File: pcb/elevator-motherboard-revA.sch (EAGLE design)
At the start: 55 parts, among them J3 MAGJACK, J4 MAGJACK, J5 MAGJACK, J6 POWER_JACK, J8 MAGJACK, Q1 NCV8403BDTRKG, Q2 MOSFET_NCH_DUAL-SO08, Q3 MOSFET_NCH_DUAL-SO08, Q4 MOSFET_NCH_DUAL-SO08, Q5 NCV8403BDTRKG, Q6 MOSFET_NCH_DUAL-SO08, Q7 NCV8403BDTRKG, Q8 NCV8403BDTRKG, Q9 NCV8403BDTRKG, U2 TPD2E001, U3 TPD2E001, U4 74HC2G125, U5 TPD2E001, U7 TPD2E001

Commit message: motherboard schematic is done
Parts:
- removed C19: 0.1uF, microbuilder:CAP_CERAMIC0603
- removed OUT4: MC4, con-phoenix-381_l:MC4
- removed PP3, PP4: MC2, con-phoenix-381_l:MC2
- added J1, J10, J7: (no value), SparkFun-Connectors:CONN_03
- added J9: (no value), SparkFun-Connectors:CONN_06NO_SILK_FEMALE_PTH
- added LED1, LED2, LED3, LED4: LED-GREEN0603, BeagleBone_Blue_R3:LED-GREEN0603
- added OUT1, OUT2: MC4, con-phoenix-381_l:MC4
- added R10, R13, R14, R7, R8, R9: (no value), adafruit:R-US_R0603
- added X1, X2, X3, X4: MSTBA2, con-phoenix-508:MSTBA2
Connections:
- new net B2B_RX1: J9.5, U$1.0/RX
- new net B2B_RX2: J9.6, U$1.2
- new net B2B_TX1: J9.3, U$1.1/TX
- new net B2B_TX2: J9.4, U$1.3/CANTX
- new net BOARD_ID: J10.2, U$1.15/A1
- new net IO1: J2.1, U$1.4/CANRX
- new net IO2: J2.2, U$1.5
- new net IO3: J2.3, U$1.6
- new net IO4: J2.4, U$1.7
- new net IO5: J2.5, U$1.12/MISO
- new net IO6: J2.6, U$1.24
- new net IO7: J2.7, U$1.25
- new net IO8: J2.8, U$1.26
- new net IO9: J2.9, U$1.27
- new net N$23: LED1.A, R9.1
- new net N$24: LED2.A, R10.1
- new net N$25: LED3.A, R7.1
- new net N$26: LED4.A, R8.1
- new net N$27: J10.3, R13.1
- new net N$33: J10.1, R14.2
- new net N$50: U$1.23/A9
- new net N$51: U$1.22/A8
- new net N$60: U$1.13/SCK
- new net N$61: U$1.GND2
- net 12V: now also J1.1, J2.10, J7.1, J7.2, OUT1.1.SK, R8.2, X3-1.1; no longer OUT4.4.SK
- net 24V: now also J1.2, J1.3, J7.3, OUT1.4.SK, OUT2.4.SK, R10.2, X1-1.1, X2-1.1; no longer PP3.1.SK, PP4.1.SK
- net 5V: now also OUT2.1.SK, R7.2, U$1.VIN, X4-1.1; no longer OUT4.1.SK
- net A.M1: now also U$1.30
- net A.M2: now also U$1.31/A12
- net A.SW1: now also U$1.28
- net A.SW2: now also U$1.29
- net B.M1: now also U$1.34/A15
- net B.M2: now also U$1.33/A14
- net B.SW1: now also U$1.32/A13
- net B.SW2: now also U$1.35/A16
- net C.M1: now also U$1.37/A18
- net C.M2: now also U$1.36/A17
- net C.SW1: now also U$1.39/A20
- net C.SW2: now also U$1.38/A19
- net D.M1: now also U$1.19/A5/SCL
- net D.M2: now also U$1.18/A4/SDA
- net D.SW1: now also U$1.9/CS
- net D.SW2: now also U$1.11/MOSI
- net GND: now also J2.12, J9.2, LED1.C, LED2.C, LED3.C, LED4.C, OUT1.2.SK, OUT1.3.SK, OUT2.2.SK, OUT2.3.SK, R14.1, X1-2.1, X2-2.1, X3-2.1, X4-2.1; no longer OUT4.2.SK, OUT4.3.SK, PP3.2.SK, PP4.2.SK
- net LEDS1: now also U$1.8
- net LEDS2: now also U$1.10/CS
- net PWM1: now also U$1.14/A0
- net PWM2: now also U$1.16/A2
- net PWM3: now also U$1.17/A3
- net PWM4: now also U$1.20/A6
- net PWM5: now also U$1.21/A7
- net VCC: now also J2.11, J9.1, R13.2, R9.2
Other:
- note added: "B2B"
- note added: "Door controller D conflicts with audio shield pins. Use one or the other!"
- note added: "Door controllers + limit switches"
- note added: "IO Panel"
- note added: "Individually addressable LEDs"
- note added: "MCU"
- note added: "PWM LEDs"
- note added: "Power rails"
- moved on the sheet: C1, C10, C11, C12, C13, C17, C18, C20, C4, C5, C6, C7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

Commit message: backup
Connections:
- new net N$34: J7.2, PP1.1.SK
- net 12V: no longer J7.2, PP1.1.SK
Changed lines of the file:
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@@
 <net name="12V" class="0">
-<segment>
-<pinref part="PP1" gate=".1" pin="SK"/>
-<wire x1="256.54" y1="320.04" x2="259.08" y2="320.04" width="0.1524" layer="91"/>
-<pinref part="J7" gate="J$1" pin="2"/>
-<wire x1="256.54" y1="320.04" x2="256.54" y2="337.82" width="0.1524" layer="91"/>
-<wire x1="256.54" y1="337.82" x2="248.92" y2="337.82" width="0.1524" layer="91"/>
-</segment>
 <segment>
 <pinref part="OUT1" gate=".1" pin="SK"/>
@@
 </segment>
 </net>
+<net name="N$34" class="0">
+<segment>
+<pinref part="J7" gate="J$1" pin="2"/>
+<pinref part="PP1" gate=".1" pin="SK"/>
+<wire x1="248.92" y1="337.82" x2="248.92" y2="320.04" width="0.1524" layer="91"/>
+<wire x1="248.92" y1="320.04" x2="259.08" y2="320.04" width="0.1524" layer="91"/>
+</segment>
+</net>

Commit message: wip
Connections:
- new net N$35: J1.2, PP2.1.SK
- net 24V: no longer J1.2, PP2.1.SK
- net GND: now also Q5.S, Q7.S, Q8.S, Q9.S
- net N$5: now also PL2.2.SK; no longer PL1.2.SK
- net N$6: now also PL1.2.SK; no longer PL2.2.SK
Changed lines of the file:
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@@
 <part name="R14" library="adafruit" library_urn="urn:adsk.eagle:library:420" deviceset="R-US_" device="R0603" package3d_urn="urn:adsk.eagle:package:6240565/1"/>
 <part name="GND12" library="SparkFun-Aesthetics" deviceset="GND" device=""/>
+<part name="U$2" library="SparkFun-PowerSymbols" library_urn="urn:adsk.eagle:library:530" deviceset="AGND" device="" value="GND"/>
 </parts>
 <sheets>
@@
 <attribute name="VALUE" x="157.48" y="15.24" size="1.778" layer="96"/>
 </instance>
+<instance part="U$2" gate="G$1" x="223.52" y="220.98" smashed="yes">
+<attribute name="VALUE" x="223.52" y="220.726" size="1.778" layer="96" align="top-center"/>
+</instance>
 </instances>
 <busses>
@@
 <wire x1="160.02" y1="20.32" x2="160.02" y2="25.4" width="0.1524" layer="91"/>
 </segment>
+<segment>
+<pinref part="U$2" gate="G$1" pin="AGND"/>
+<pinref part="Q5" gate="G$1" pin="S"/>
+<wire x1="213.36" y1="269.24" x2="223.52" y2="269.24" width="0.1524" layer="91"/>
+<wire x1="223.52" y1="269.24" x2="223.52" y2="254" width="0.1524" layer="91"/>
+<pinref part="Q7" gate="G$1" pin="S"/>
+<wire x1="223.52" y1="254" x2="223.52" y2="238.76" width="0.1524" layer="91"/>
+<wire x1="223.52" y1="238.76" x2="223.52" y2="223.52" width="0.1524" layer="91"/>
+<wire x1="213.36" y1="254" x2="223.52" y2="254" width="0.1524" layer="91"/>
+<junction x="223.52" y="254"/>
+<pinref part="Q8" gate="G$1" pin="S"/>
+<wire x1="213.36" y1="238.76" x2="223.52" y2="238.76" width="0.1524" layer="91"/>
+<junction x="223.52" y="238.76"/>
+<pinref part="Q9" gate="G$1" pin="S"/>
+<wire x1="213.36" y1="223.52" x2="223.52" y2="223.52" width="0.1524" layer="91"/>
+<junction x="223.52" y="223.52"/>
+</segment>
 </net>
 <net name="12V" class="0">
@@
 </segment>
 </net>
-<net name="N$5" class="0">
-<segment>
-<pinref part="U4" gate="G$1" pin="1Y"/>
-<wire x1="220.98" y1="137.16" x2="238.76" y2="137.16" width="0.1524" layer="91"/>
-<wire x1="238.76" y1="149.86" x2="238.76" y2="137.16" width="0.1524" layer="91"/>
-<pinref part="PL1" gate=".2" pin="SK"/>
-<wire x1="238.76" y1="149.86" x2="271.78" y2="149.86" width="0.1524" layer="91"/>
-</segment>
-</net>
-<net name="N$6" class="0">
-<segment>
-<pinref part="U4" gate="G$1" pin="2Y"/>
-<pinref part="PL2" gate=".2" pin="SK"/>
-<wire x1="271.78" y1="121.92" x2="259.08" y2="121.92" width="0.1524" layer="91"/>
-<wire x1="259.08" y1="121.92" x2="259.08" y2="129.54" width="0.1524" layer="91"/>
-<wire x1="259.08" y1="129.54" x2="220.98" y2="129.54" width="0.1524" layer="91"/>
-</segment>
-</net>
 <net name="LEDS1" class="0">
 <segment>
@@
 <net name="24V" class="0">
 <segment>
-<pinref part="PP2" gate=".1" pin="SK"/>
-<wire x1="256.54" y1="266.7" x2="261.62" y2="266.7" width="0.1524" layer="91"/>
-<pinref part="J1" gate="J$1" pin="2"/>
-<wire x1="251.46" y1="292.1" x2="256.54" y2="292.1" width="0.1524" layer="91"/>
-<wire x1="256.54" y1="292.1" x2="256.54" y2="266.7" width="0.1524" layer="91"/>
-</segment>
-<segment>
 <pinref part="J6" gate="G$1" pin="PWR"/>
 <wire x1="111.76" y1="320.04" x2="119.38" y2="320.04" width="0.1524" layer="91"/>
@@
 </segment>
 </net>
+<net name="N$35" class="0">
+<segment>
+<pinref part="J1" gate="J$1" pin="2"/>
+<wire x1="251.46" y1="292.1" x2="259.08" y2="292.1" width="0.1524" layer="91"/>
+<wire x1="259.08" y1="292.1" x2="259.08" y2="266.7" width="0.1524" layer="91"/>
+<pinref part="PP2" gate=".1" pin="SK"/>
+<wire x1="259.08" y1="266.7" x2="261.62" y2="266.7" width="0.1524" layer="91"/>
+</segment>
+</net>
+<net name="N$5" class="0">
+<segment>
+<pinref part="U4" gate="G$1" pin="1Y"/>
+<wire x1="220.98" y1="137.16" x2="256.54" y2="137.16" width="0.1524" layer="91"/>
+<wire x1="256.54" y1="137.16" x2="256.54" y2="121.92" width="0.1524" layer="91"/>
+<pinref part="PL2" gate=".2" pin="SK"/>
+<wire x1="256.54" y1="121.92" x2="271.78" y2="121.92" width="0.1524" layer="91"/>
+</segment>
+</net>
+<net name="N$6" class="0">
+<segment>
+<pinref part="U4" gate="G$1" pin="2Y"/>
+<wire x1="220.98" y1="129.54" x2="241.3" y2="129.54" width="0.1524" layer="91"/>
+<wire x1="241.3" y1="129.54" x2="241.3" y2="149.86" width="0.1524" layer="91"/>
+<pinref part="PL1" gate=".2" pin="SK"/>
+<wire x1="241.3" y1="149.86" x2="271.78" y2="149.86" width="0.1524" layer="91"/>
+</segment>
+</net>

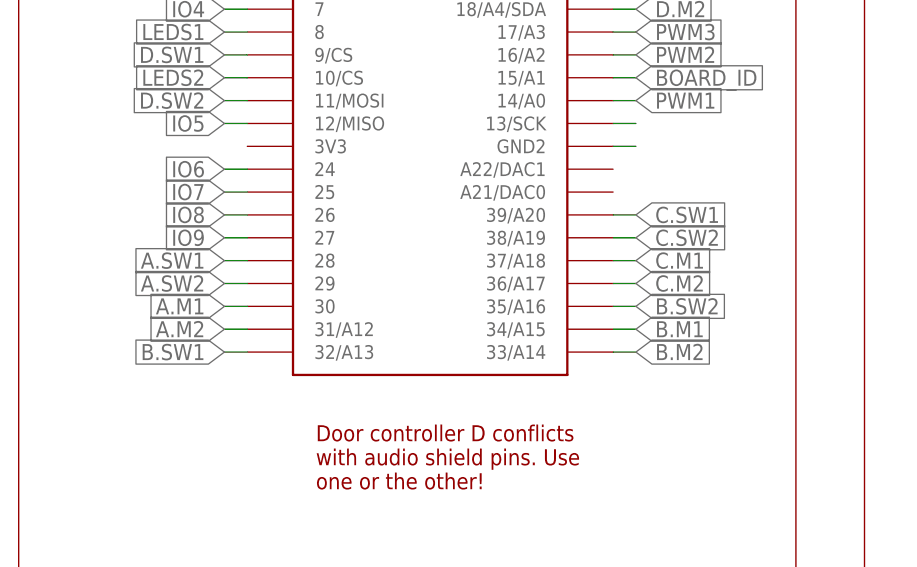
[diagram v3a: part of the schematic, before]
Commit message: better placement
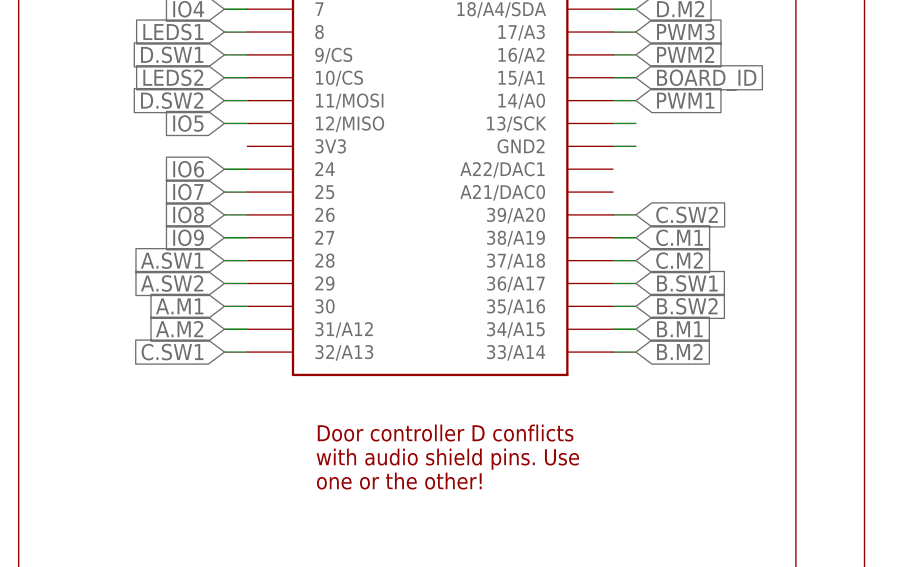
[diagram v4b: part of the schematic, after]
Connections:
- net B.SW1: now also U$1.36/A17; no longer U$1.32/A13
- net C.M1: now also U$1.38/A19; no longer U$1.37/A18
- net C.M2: now also U$1.37/A18; no longer U$1.36/A17
- net C.SW1: now also U$1.32/A13; no longer U$1.39/A20
- net C.SW2: now also U$1.39/A20; no longer U$1.38/A19
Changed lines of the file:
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@@
 </segment>
 <segment>
-<pinref part="U$1" gate="G$1" pin="32/A13"/>
-<wire x1="63.5" y1="30.48" x2="60.96" y2="30.48" width="0.1524" layer="91"/>
-<label x="60.96" y="30.48" size="1.778" layer="95" rot="R180" xref="yes"/>
+<pinref part="U$1" gate="G$1" pin="36/A17"/>
+<wire x1="104.14" y1="38.1" x2="106.68" y2="38.1" width="0.1524" layer="91"/>
+<label x="106.68" y="38.1" size="1.778" layer="95" xref="yes"/>
 </segment>
 </net>
@@
 </segment>
 <segment>
-<pinref part="U$1" gate="G$1" pin="39/A20"/>
-<wire x1="104.14" y1="45.72" x2="106.68" y2="45.72" width="0.1524" layer="91"/>
-<label x="106.68" y="45.72" size="1.778" layer="95" xref="yes"/>
+<pinref part="U$1" gate="G$1" pin="32/A13"/>
+<wire x1="63.5" y1="30.48" x2="60.96" y2="30.48" width="0.1524" layer="91"/>
+<label x="60.96" y="30.48" size="1.778" layer="95" rot="R180" xref="yes"/>
 </segment>
 </net>
@@
 </segment>
 <segment>
-<pinref part="U$1" gate="G$1" pin="38/A19"/>
-<wire x1="104.14" y1="43.18" x2="106.68" y2="43.18" width="0.1524" layer="91"/>
-<label x="106.68" y="43.18" size="1.778" layer="95" xref="yes"/>
+<pinref part="U$1" gate="G$1" pin="39/A20"/>
+<wire x1="104.14" y1="45.72" x2="106.68" y2="45.72" width="0.1524" layer="91"/>
+<label x="106.68" y="45.72" size="1.778" layer="95" xref="yes"/>
 </segment>
 </net>
@@
 </segment>
 <segment>
-<pinref part="U$1" gate="G$1" pin="37/A18"/>
-<wire x1="104.14" y1="40.64" x2="106.68" y2="40.64" width="0.1524" layer="91"/>
-<label x="106.68" y="40.64" size="1.778" layer="95" xref="yes"/>
+<pinref part="U$1" gate="G$1" pin="38/A19"/>
+<wire x1="104.14" y1="43.18" x2="106.68" y2="43.18" width="0.1524" layer="91"/>
+<label x="106.68" y="43.18" size="1.778" layer="95" xref="yes"/>
 </segment>
 </net>
@@
 </segment>
 <segment>
-<pinref part="U$1" gate="G$1" pin="36/A17"/>
-<wire x1="104.14" y1="38.1" x2="106.68" y2="38.1" width="0.1524" layer="91"/>
-<label x="106.68" y="38.1" size="1.778" layer="95" xref="yes"/>
+<pinref part="U$1" gate="G$1" pin="37/A18"/>
+<wire x1="104.14" y1="40.64" x2="106.68" y2="40.64" width="0.1524" layer="91"/>
+<label x="106.68" y="40.64" size="1.778" layer="95" xref="yes"/>
 </segment>
 </net>

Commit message: wip
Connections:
- removed net N$61: U$1.GND2
- net GND: now also U$1.GND, U$1.GND2
- net IO1: now also U$1.6; no longer U$1.4/CANRX
- net IO2: now also U$1.7; no longer U$1.5
- net IO3: now also U$1.5; no longer U$1.6
- net IO4: now also U$1.12/MISO; no longer U$1.7
- net IO5: now also U$1.4/CANRX; no longer U$1.12/MISO
- net IO7: now also U$1.27; no longer U$1.25
- net IO8: now also U$1.25; no longer U$1.26
- net IO9: now also U$1.26; no longer U$1.27
- net VCC: now also U$1.3V3
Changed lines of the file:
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@@
 <junction x="223.52" y="223.52"/>
+</segment>
+<segment>
+<pinref part="U$1" gate="G$1" pin="GND2"/>
+<wire x1="104.14" y1="53.34" x2="106.68" y2="53.34" width="0.1524" layer="91"/>
+<label x="106.68" y="53.34" size="1.778" layer="95" xref="yes"/>
+</segment>
+<segment>
+<pinref part="U$1" gate="G$1" pin="GND"/>
+<wire x1="63.5" y1="88.9" x2="60.96" y2="88.9" width="0.1524" layer="91"/>
+<label x="60.96" y="88.9" size="1.778" layer="95" rot="R180" xref="yes"/>
 </segment>
 </net>
@@
 <label x="160.02" y="60.96" size="2.54" layer="95" rot="R90" xref="yes"/>
 </segment>
+<segment>
+<pinref part="U$1" gate="G$1" pin="3V3"/>
+<wire x1="63.5" y1="53.34" x2="48.26" y2="53.34" width="0.1524" layer="91"/>
+<label x="48.26" y="53.34" size="1.778" layer="95" rot="R180" xref="yes"/>
+</segment>
 </net>
 <net name="N$1" class="0">
@@
 <net name="IO1" class="0">
 <segment>
+<pinref part="J2" gate="G$1" pin="1"/>
+<wire x1="203.2" y1="38.1" x2="198.12" y2="38.1" width="0.1524" layer="91"/>
+<label x="198.12" y="38.1" size="1.778" layer="95" rot="R180" xref="yes"/>
+</segment>
+<segment>
+<pinref part="U$1" gate="G$1" pin="6"/>
+<wire x1="63.5" y1="71.12" x2="60.96" y2="71.12" width="0.1524" layer="91"/>
+<label x="60.96" y="71.12" size="1.778" layer="95" rot="R180" xref="yes"/>
+</segment>
+</net>
+<net name="IO2" class="0">
+<segment>
+<pinref part="J2" gate="G$1" pin="2"/>
+<wire x1="218.44" y1="38.1" x2="223.52" y2="38.1" width="0.1524" layer="91"/>
+<label x="223.52" y="38.1" size="1.778" layer="95" xref="yes"/>
+</segment>
+<segment>
+<pinref part="U$1" gate="G$1" pin="7"/>
+<wire x1="63.5" y1="68.58" x2="60.96" y2="68.58" width="0.1524" layer="91"/>
+<label x="60.96" y="68.58" size="1.778" layer="95" rot="R180" xref="yes"/>
+</segment>
+</net>
+<net name="IO3" class="0">
+<segment>
+<pinref part="J2" gate="G$1" pin="3"/>
+<wire x1="203.2" y1="35.56" x2="198.12" y2="35.56" width="0.1524" layer="91"/>
+<label x="198.12" y="35.56" size="1.778" layer="95" rot="R180" xref="yes"/>
+</segment>
+<segment>
+<pinref part="U$1" gate="G$1" pin="5"/>
+<wire x1="63.5" y1="73.66" x2="60.96" y2="73.66" width="0.1524" layer="91"/>
+<label x="60.96" y="73.66" size="1.778" layer="95" rot="R180" xref="yes"/>
+</segment>
+</net>
+<net name="IO4" class="0">
+<segment>
+<pinref part="J2" gate="G$1" pin="4"/>
+<wire x1="218.44" y1="35.56" x2="223.52" y2="35.56" width="0.1524" layer="91"/>
+<label x="223.52" y="35.56" size="1.778" layer="95" xref="yes"/>
+</segment>
+<segment>
+<pinref part="U$1" gate="G$1" pin="12/MISO"/>
+<wire x1="63.5" y1="55.88" x2="60.96" y2="55.88" width="0.1524" layer="91"/>
+<label x="60.96" y="55.88" size="1.778" layer="95" rot="R180" xref="yes"/>
+</segment>
+</net>
+<net name="IO5" class="0">
+<segment>
+<pinref part="J2" gate="G$1" pin="5"/>
+<wire x1="203.2" y1="33.02" x2="198.12" y2="33.02" width="0.1524" layer="91"/>
+<label x="198.12" y="33.02" size="1.778" layer="95" rot="R180" xref="yes"/>
+</segment>
+<segment>
 <pinref part="U$1" gate="G$1" pin="4/CANRX"/>
 <wire x1="63.5" y1="76.2" x2="60.96" y2="76.2" width="0.1524" layer="91"/>
 <label x="60.96" y="76.2" size="1.778" layer="95" rot="R180" xref="yes"/>
 </segment>
-<segment>
-<pinref part="J2" gate="G$1" pin="1"/>
-<wire x1="203.2" y1="38.1" x2="198.12" y2="38.1" width="0.1524" layer="91"/>
-<label x="198.12" y="38.1" size="1.778" layer="95" rot="R180" xref="yes"/>
-</segment>
-</net>
-<net name="IO2" class="0">
-<segment>
-<pinref part="U$1" gate="G$1" pin="5"/>
-<wire x1="63.5" y1="73.66" x2="60.96" y2="73.66" width="0.1524" layer="91"/>
-<label x="60.96" y="73.66" size="1.778" layer="95" rot="R180" xref="yes"/>
-</segment>
-<segment>
-<pinref part="J2" gate="G$1" pin="2"/>
-<wire x1="218.44" y1="38.1" x2="223.52" y2="38.1" width="0.1524" layer="91"/>
-<label x="223.52" y="38.1" size="1.778" layer="95" xref="yes"/>
-</segment>
-</net>
-<net name="IO3" class="0">
-<segment>
-<pinref part="U$1" gate="G$1" pin="6"/>
-<wire x1="63.5" y1="71.12" x2="60.96" y2="71.12" width="0.1524" layer="91"/>
-<label x="60.96" y="71.12" size="1.778" layer="95" rot="R180" xref="yes"/>
-</segment>
-<segment>
-<pinref part="J2" gate="G$1" pin="3"/>
-<wire x1="203.2" y1="35.56" x2="198.12" y2="35.56" width="0.1524" layer="91"/>
-<label x="198.12" y="35.56" size="1.778" layer="95" rot="R180" xref="yes"/>
-</segment>
-</net>
-<net name="IO4" class="0">
-<segment>
-<pinref part="U$1" gate="G$1" pin="7"/>
-<wire x1="63.5" y1="68.58" x2="60.96" y2="68.58" width="0.1524" layer="91"/>
-<label x="60.96" y="68.58" size="1.778" layer="95" rot="R180" xref="yes"/>
-</segment>
-<segment>
-<pinref part="J2" gate="G$1" pin="4"/>
-<wire x1="218.44" y1="35.56" x2="223.52" y2="35.56" width="0.1524" layer="91"/>
-<label x="223.52" y="35.56" size="1.778" layer="95" xref="yes"/>
-</segment>
-</net>
-<net name="IO5" class="0">
-<segment>
-<pinref part="U$1" gate="G$1" pin="12/MISO"/>
-<wire x1="63.5" y1="55.88" x2="60.96" y2="55.88" width="0.1524" layer="91"/>
-<label x="60.96" y="55.88" size="1.778" layer="95" rot="R180" xref="yes"/>
-</segment>
-<segment>
-<pinref part="J2" gate="G$1" pin="5"/>
-<wire x1="203.2" y1="33.02" x2="198.12" y2="33.02" width="0.1524" layer="91"/>
-<label x="198.12" y="33.02" size="1.778" layer="95" rot="R180" xref="yes"/>
-</segment>
 </net>
 <net name="IO6" class="0">
@@
 <net name="IO7" class="0">
 <segment>
+<pinref part="J2" gate="G$1" pin="7"/>
+<wire x1="203.2" y1="30.48" x2="198.12" y2="30.48" width="0.1524" layer="91"/>
+<label x="198.12" y="30.48" size="1.778" layer="95" rot="R180" xref="yes"/>
+</segment>
+<segment>
+<pinref part="U$1" gate="G$1" pin="27"/>
+<wire x1="63.5" y1="43.18" x2="60.96" y2="43.18" width="0.1524" layer="91"/>
+<label x="60.96" y="43.18" size="1.778" layer="95" rot="R180" xref="yes"/>
+</segment>
+</net>
+<net name="IO8" class="0">
+<segment>
+<pinref part="J2" gate="G$1" pin="8"/>
+<wire x1="218.44" y1="30.48" x2="223.52" y2="30.48" width="0.1524" layer="91"/>
+<label x="223.52" y="30.48" size="1.778" layer="95" xref="yes"/>
+</segment>
+<segment>
 <pinref part="U$1" gate="G$1" pin="25"/>
 <wire x1="63.5" y1="48.26" x2="60.96" y2="48.26" width="0.1524" layer="91"/>
 <label x="60.96" y="48.26" size="1.778" layer="95" rot="R180" xref="yes"/>
 </segment>
-<segment>
-<pinref part="J2" gate="G$1" pin="7"/>
-<wire x1="203.2" y1="30.48" x2="198.12" y2="30.48" width="0.1524" layer="91"/>
-<label x="198.12" y="30.48" size="1.778" layer="95" rot="R180" xref="yes"/>
-</segment>
-</net>
-<net name="IO8" class="0">
+</net>
+<net name="IO9" class="0">
+<segment>
+<pinref part="J2" gate="G$1" pin="9"/>
+<wire x1="203.2" y1="27.94" x2="198.12" y2="27.94" width="0.1524" layer="91"/>
+<label x="198.12" y="27.94" size="1.778" layer="95" rot="R180" xref="yes"/>
+</segment>
 <segment>
 <pinref part="U$1" gate="G$1" pin="26"/>
@@
 <label x="60.96" y="45.72" size="1.778" layer="95" rot="R180" xref="yes"/>
 </segment>
-<segment>
-<pinref part="J2" gate="G$1" pin="8"/>
-<wire x1="218.44" y1="30.48" x2="223.52" y2="30.48" width="0.1524" layer="91"/>
-<label x="223.52" y="30.48" size="1.778" layer="95" xref="yes"/>
-</segment>
-</net>
-<net name="IO9" class="0">
-<segment>
-<pinref part="U$1" gate="G$1" pin="27"/>
-<wire x1="63.5" y1="43.18" x2="60.96" y2="43.18" width="0.1524" layer="91"/>
-<label x="60.96" y="43.18" size="1.778" layer="95" rot="R180" xref="yes"/>
-</segment>
-<segment>
-<pinref part="J2" gate="G$1" pin="9"/>
-<wire x1="203.2" y1="27.94" x2="198.12" y2="27.94" width="0.1524" layer="91"/>
-<label x="198.12" y="27.94" size="1.778" layer="95" rot="R180" xref="yes"/>
-</segment>
 </net>
 <net name="N$50" class="0">
@@
 </segment>
 </net>
-<net name="N$61" class="0">
-<segment>
-<pinref part="U$1" gate="G$1" pin="GND2"/>
-<wire x1="104.14" y1="53.34" x2="106.68" y2="53.34" width="0.1524" layer="91"/>
-</segment>
-</net>
